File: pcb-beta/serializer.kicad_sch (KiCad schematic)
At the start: 26 parts, among them U3 DS90UB933TRTVTQ1

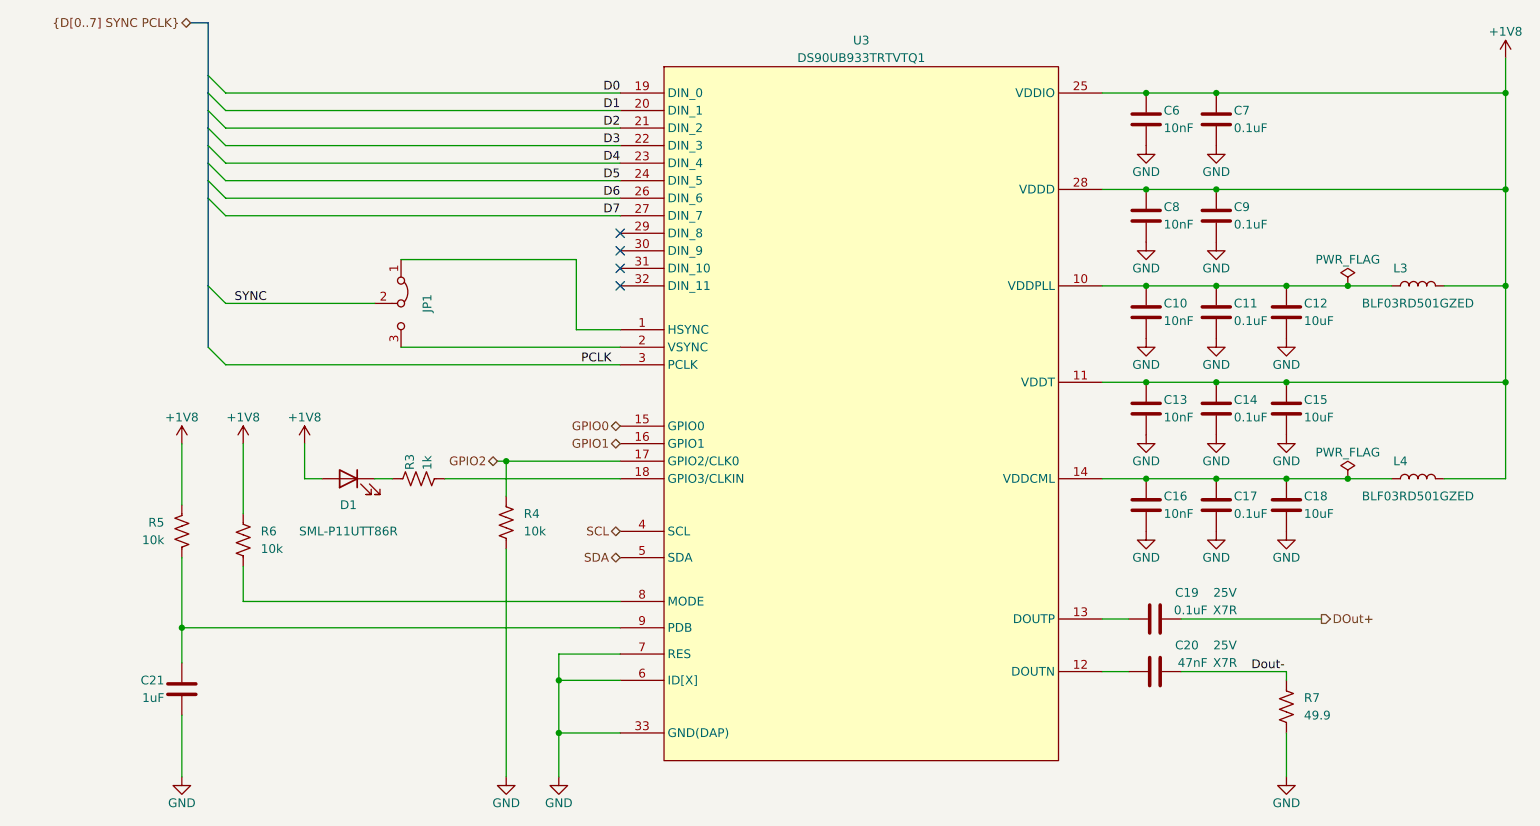
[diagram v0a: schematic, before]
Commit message: Move pcb to pcb-beta directory
- Because this board only works with Beta-test NP2.0 probes
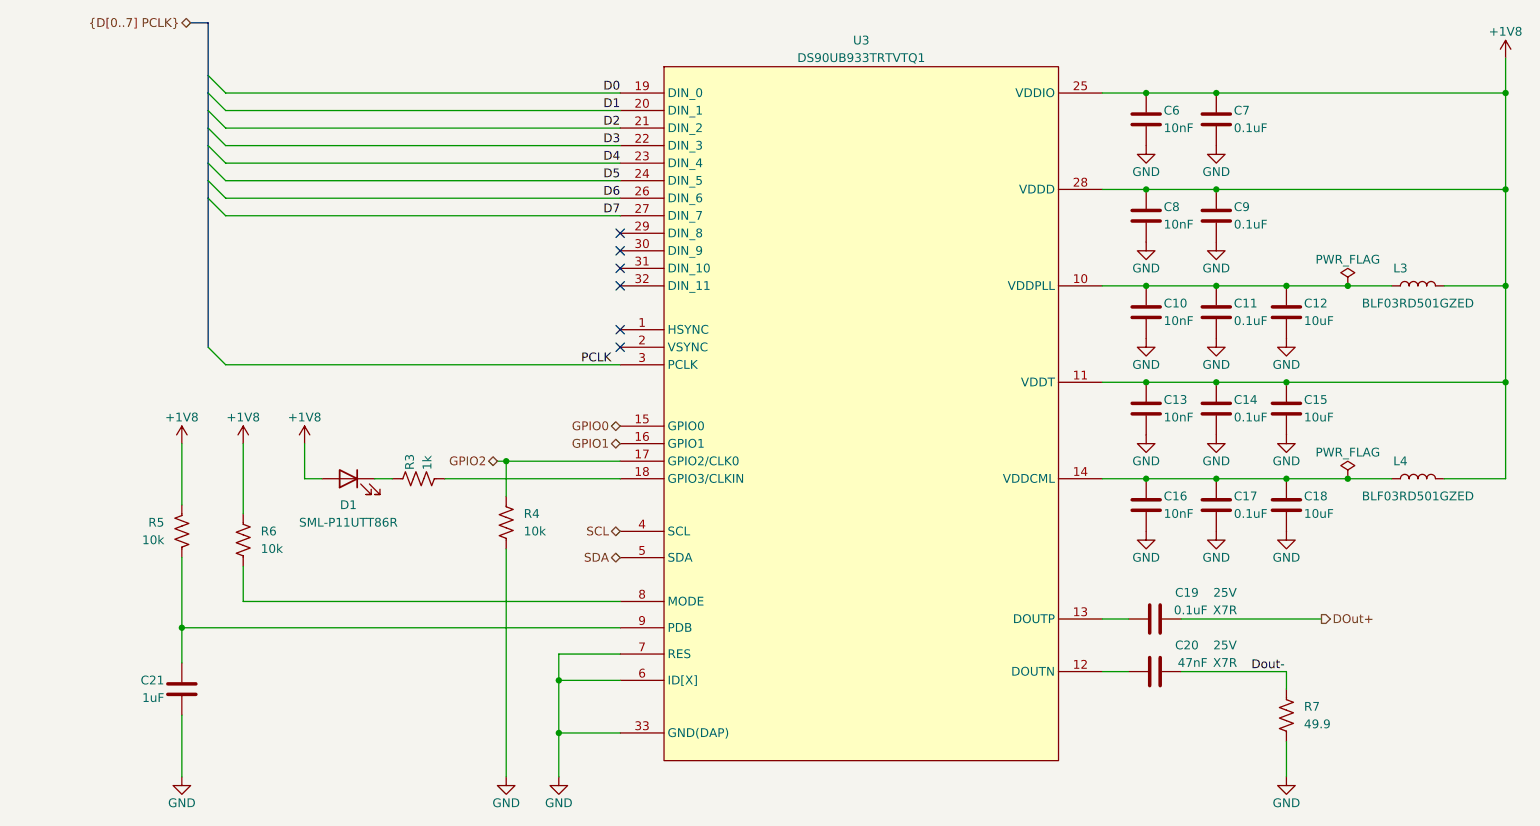
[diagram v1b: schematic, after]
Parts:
- removed JP1: Jumper_3_Bridged12, jonnew:OE_SolderJumper-3_0201_Bridged12, symbol Jumper:Jumper_3_Bridged12
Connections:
- no-connect marks 4 -> 6
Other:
- moved on the sheet: R7
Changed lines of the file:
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@@
   (junction (at 196.85 48.26) (diameter 0) (color 0 0 0 0)
   )
+  (no_connect (at 120.65 82.55))
   (no_connect (at 120.65 76.2))
   (no_connect (at 120.65 71.12))
   (no_connect (at 120.65 73.66))
+  (no_connect (at 120.65 85.09))
   (no_connect (at 120.65 68.58))
   (bus_entry (at 60.96 58.42) (size 2.54 2.54)
     (stroke (width 0) (type default))
   )
-  (bus_entry (at 60.96 76.2) (size 2.54 2.54)
-    (stroke (width 0) (type default))
-  )
   (bus_entry (at 60.96 85.09) (size 2.54 2.54)
     (stroke (width 0) (type default))
@@
     (stroke (width 0) (type default))
   )
-  (wire (pts (xy 114.3 72.39) (xy 114.3 82.55))
-    (stroke (width 0) (type default))
-  )
   (wire (pts (xy 111.76 129.54) (xy 111.76 133.35))
     (stroke (width 0) (type default))
   )
-  (bus (pts (xy 60.96 85.09) (xy 60.96 76.2))
-    (stroke (width 0) (type default))
-  )
   (wire (pts (xy 63.5 66.04) (xy 120.65 66.04))
     (stroke (width 0) (type default))
@@
     (stroke (width 0) (type default))
   )
-  (wire (pts (xy 114.3 82.55) (xy 120.65 82.55))
-    (stroke (width 0) (type default))
-  )
   (wire (pts (xy 190.5 90.17) (xy 196.85 90.17))
     (stroke (width 0) (type default))
@@
     (stroke (width 0) (type default))
   )
-  (wire (pts (xy 63.5 78.74) (xy 85.09 78.74))
-    (stroke (width 0) (type default))
-  )
   (wire (pts (xy 201.93 124.46) (xy 222.25 124.46))
     (stroke (width 0) (type default))
@@
     (stroke (width 0) (type default))
   )
-  (wire (pts (xy 88.9 85.09) (xy 120.65 85.09))
-    (stroke (width 0) (type default))
-  )
-  (bus (pts (xy 60.96 76.2) (xy 60.96 63.5))
+  (bus (pts (xy 60.96 63.5) (xy 60.96 85.09))
     (stroke (width 0) (type default))
   )
@@
     (stroke (width 0) (type default))
   )
-  (wire (pts (xy 217.17 140.97) (xy 217.17 147.32))
+  (wire (pts (xy 217.17 142.24) (xy 217.17 147.32))
     (stroke (width 0) (type default))
   )
@@
     (stroke (width 0) (type default))
   )
-  (wire (pts (xy 217.17 132.08) (xy 217.17 133.35))
+  (wire (pts (xy 217.17 132.08) (xy 217.17 134.62))
     (stroke (width 0) (type default))
   )
@@
   )
   (bus (pts (xy 60.96 55.88) (xy 60.96 53.34))
-    (stroke (width 0) (type default))
-  )
-  (wire (pts (xy 88.9 72.39) (xy 114.3 72.39))
     (stroke (width 0) (type default))
   )
@@
     (effects (font (size 1.27 1.27)) (justify left bottom))
   )
-  (label "SYNC" (at 64.77 78.74 0) (fields_autoplaced)
-    (effects (font (size 1.27 1.27)) (justify left bottom))
-  )
   (label "PCLK" (at 119.38 87.63 180) (fields_autoplaced)
     (effects (font (size 1.27 1.27)) (justify right bottom))
@@
     (effects (font (size 1.27 1.27)) (justify right))
   )
-  (hierarchical_label "{D[0..7] SYNC PCLK}" (shape bidirectional) (at 58.42 38.1 180) (fields_autoplaced)
+  (hierarchical_label "{D[0..7] PCLK}" (shape bidirectional) (at 58.42 38.1 180) (fields_autoplaced)
     (effects (font (size 1.27 1.27)) (justify right))
   )
@@
     )
   )
-  (symbol (lib_id "Device:R_US") (at 217.17 137.16 0) (unit 1)
-    (in_bom yes) (on_board yes) (dnp no)
-    (property "Reference" "R7" (at 219.71 135.89 0)
-      (effects (font (size 1.27 1.27)) (justify left))
-    )
-    (property "Value" "49.9" (at 219.71 138.43 0)
-      (effects (font (size 1.27 1.27)) (justify left))
-    )
-    (property "Footprint" "Resistor_SMD:R_0201_0603Metric" (at 218.186 137.414 90)
-      (effects (font (size 1.27 1.27)) hide)
-    )
-    (property "Datasheet" "~" (at 217.17 137.16 0)
-      (effects (font (size 1.27 1.27)) hide)
-    )
-    (property "CASE/PACKAGE" "0201" (at 217.17 137.16 0)
-      (effects (font (size 1.27 1.27)) hide)
-    )
-    (property "Tolerance" "1%" (at 217.17 137.16 0)
+  (symbol (lib_id "Device:R_US") (at 217.17 138.43 0) (unit 1)
+    (in_bom yes) (on_board yes) (dnp no)
+    (property "Reference" "R7" (at 219.71 137.16 0)
+      (effects (font (size 1.27 1.27)) (justify left))
+    )
+    (property "Value" "49.9" (at 219.71 139.7 0)
+      (effects (font (size 1.27 1.27)) (justify left))
+    )
+    (property "Footprint" "Resistor_SMD:R_0201_0603Metric" (at 218.186 138.684 90)
+      (effects (font (size 1.27 1.27)) hide)
+    )
+    (property "Datasheet" "~" (at 217.17 138.43 0)
+      (effects (font (size 1.27 1.27)) hide)
+    )
+    (property "CASE/PACKAGE" "0201" (at 217.17 138.43 0)
+      (effects (font (size 1.27 1.27)) hide)
+    )
+    (property "Tolerance" "1%" (at 217.17 138.43 0)
       (effects (font (size 1.27 1.27)) hide)
     )
@@
         (path "/8b149c2d-f56a-45f8-a6f1-7a24c86142b6/9dea7771-d871-4129-9ad1-7b3654fe6f0e"
           (reference "#PWR030") (unit 1)
-        )
-      )
-    )
-  )
-  (symbol (lib_id "Jumper:Jumper_3_Bridged12") (at 88.9 78.74 270) (unit 1)
-    (in_bom no) (on_board yes) (dnp no)
-    (property "Reference" "JP1" (at 92.71 78.74 0)
-      (effects (font (size 1.27 1.27)))
-    )
-    (property "Value" "Jumper_3_Bridged12" (at 82.55 74.93 0)
-      (effects (font (size 1.27 1.27)) hide)
-    )
-    (property "Footprint" "jonnew:OE_SolderJumper-3_0201_Bridged12" (at 88.9 78.74 0)
-      (effects (font (size 1.27 1.27)) hide)
-    )
-    (property "Datasheet" "~" (at 88.9 78.74 0)
-      (effects (font (size 1.27 1.27)) hide)
-    )
-    (property "Tolerance" "" (at 88.9 78.74 0)
-      (effects (font (size 1.27 1.27)) hide)
-    )
-    (pin "1")
-    (pin "2")
-    (pin "3")
-    (instances
-      (project "headstage-neuropix2e"
-        (path "/8b149c2d-f56a-45f8-a6f1-7a24c86142b6/9dea7771-d871-4129-9ad1-7b3654fe6f0e"
-          (reference "JP1") (unit 1)
         )
       )
@@
       (effects (font (size 1.27 1.27)))
     )
-    (property "Value" "SML-P11UTT86R" (at 81.28 111.76 0)
-      (effects (font (size 1.27 1.27)))
-    )
+    (property "Value" "SML-P11UTT86R" (at 81.28 110.49 0)
+      (effects (font (size 1.27 1.27)))
+    )
